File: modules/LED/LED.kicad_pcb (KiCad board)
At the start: 2 copper layers, 40.6 x 40.6 mm, 54 parts, among them J1 2, J10 11, J11 12, J12 13, J13 A0, J14 A1, J15 A2, J16 A3, J17 A4, J18 A5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

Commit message: Fix 74LS139 pins
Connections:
- U2 pad 13: /A0 -> /A1
- U2 pad 14: /A1 -> /A0
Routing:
- net /A1: track 17.6 -> 12.7 mm, vias 2 -> 0
- net /A0: track 11.5 -> 10.2 mm
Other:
- board text added: "07.11.2020"
- board text added: "v2.1"
- board text removed: "08.04.2020"
- board text removed: "v2"

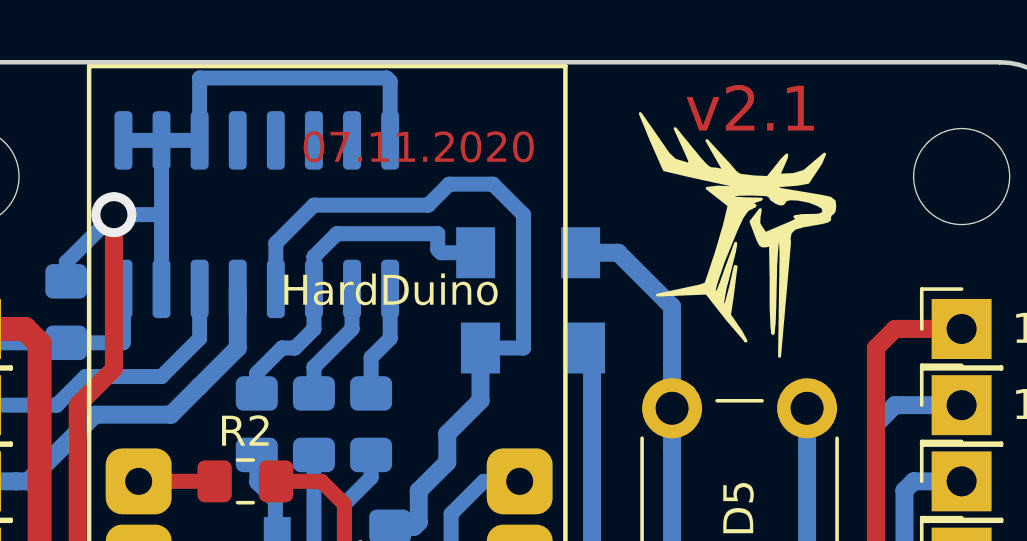
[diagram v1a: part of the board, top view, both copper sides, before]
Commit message: Add hash, fix labels
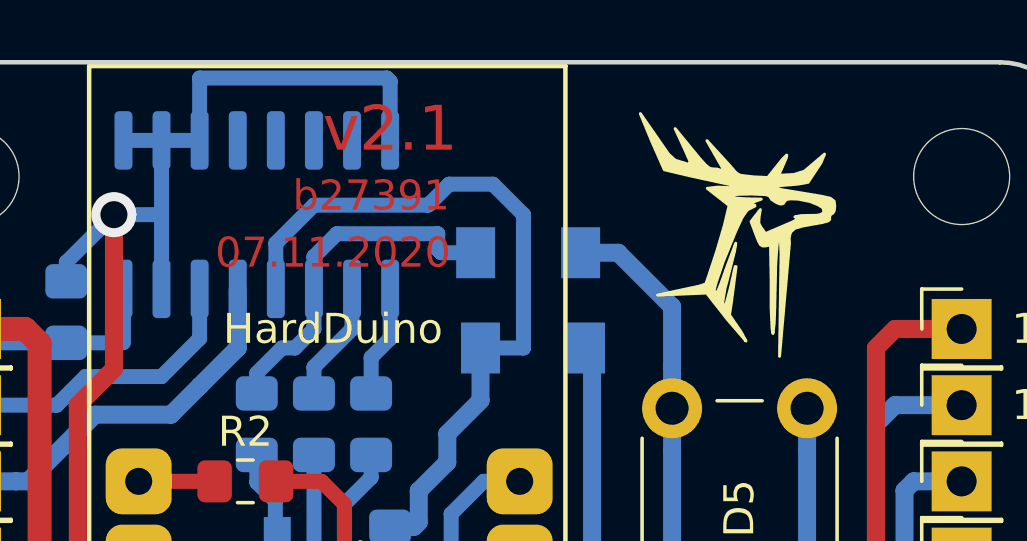
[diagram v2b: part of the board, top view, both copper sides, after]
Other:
- board text added: "b27391"

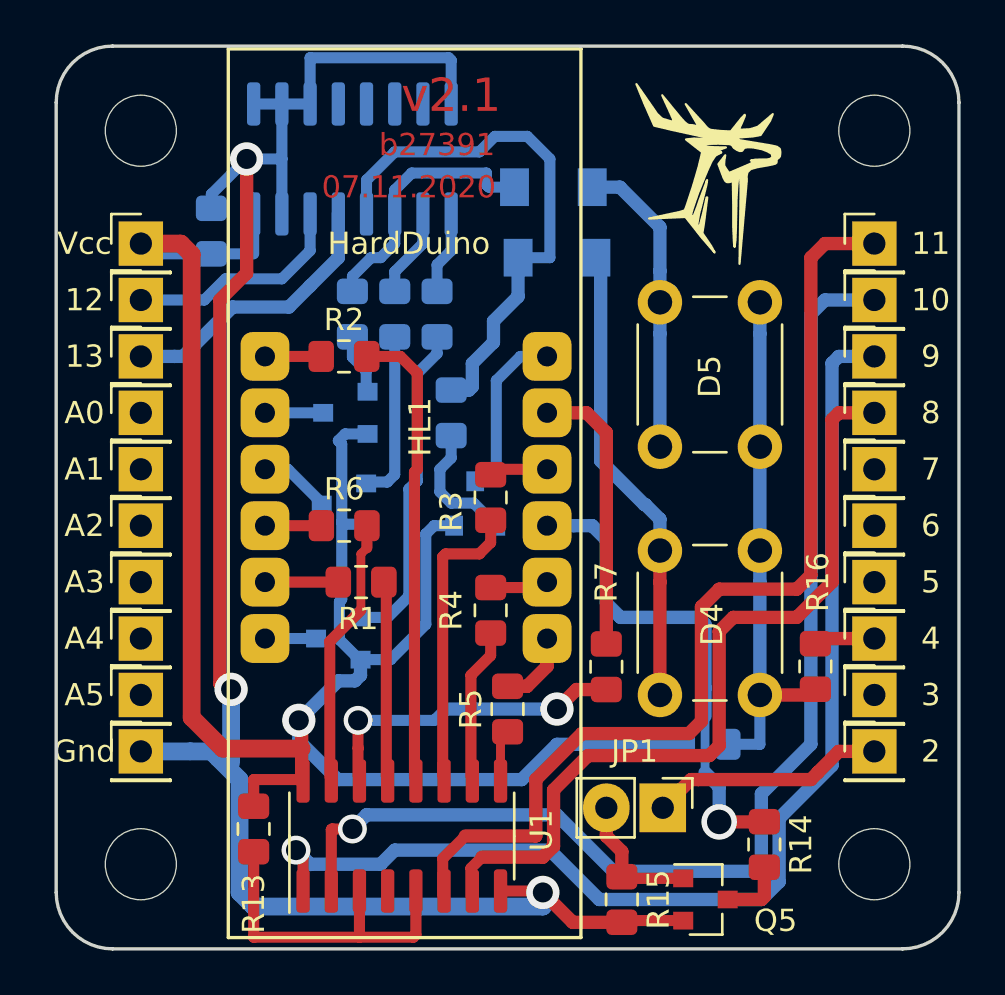
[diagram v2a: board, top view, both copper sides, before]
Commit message: Add legend to LED
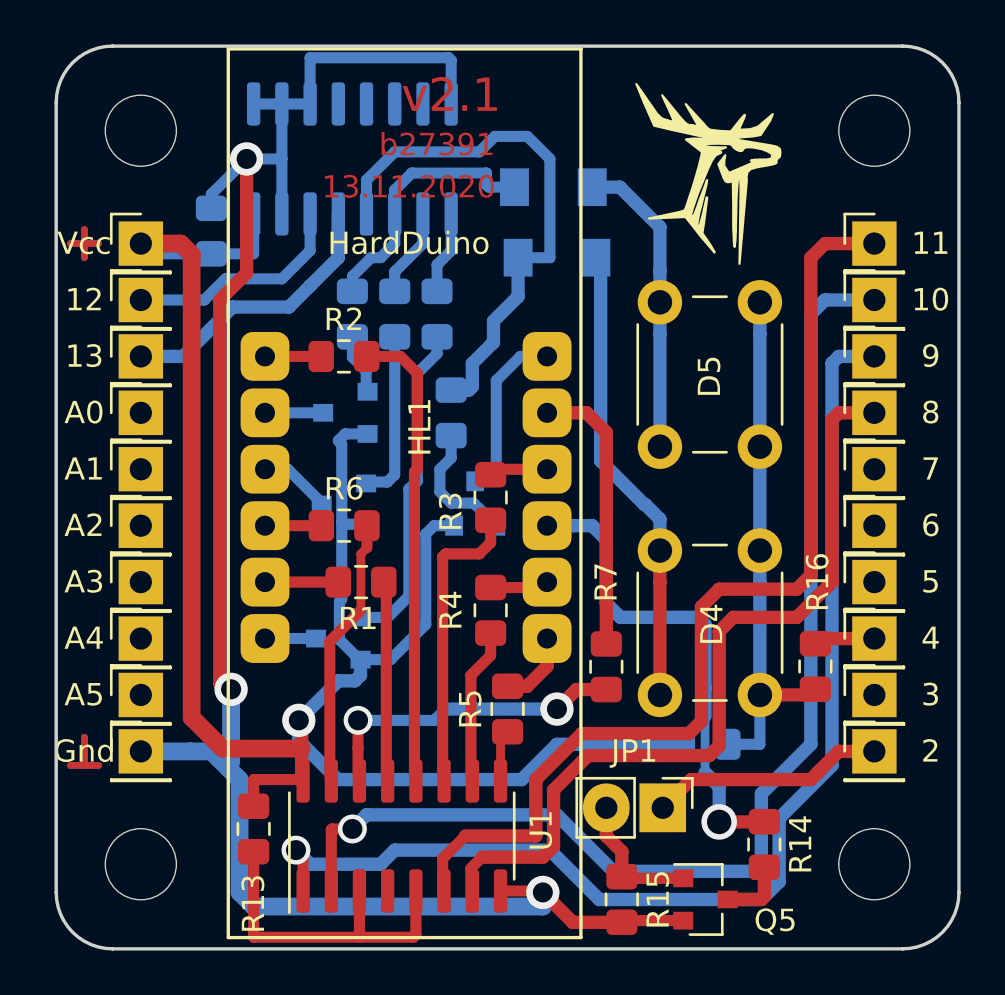
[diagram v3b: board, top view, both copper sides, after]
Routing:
- net (no net): track 0.00 -> 10.2 mm
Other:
- rule solder_mask_min_width: 0.25 -> 0.1
- board text added: "13.11.2020"
- board text added: "D0"
- board text added: "D1"
- board text added: "D2"
- board text added: "D3"
- board text added: "DP"
- board text added: "L0"
- board text removed: "07.11.2020"
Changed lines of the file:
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@@
   (general
     (thickness 1.6)
-    (drawings 33)
-    (tracks 319)
+    (drawings 41)
+    (tracks 327)
     (zones 0)
     (modules 54)
@@
     (pad_drill 1)
     (pad_to_mask_clearance 0.051)
-    (solder_mask_min_width 0.25)
+    (solder_mask_min_width 0.1)
     (aux_axis_origin 0 0)
     (visible_elements 7FFFFFFF)
@@
     )
   )
+  (gr_text A1 (at 90.17 64.77) (layer B.SilkS)
+    (effects (font (size 1 1) (thickness 0.15)) (justify mirror))
+  )
+  (gr_text A0 (at 90.17 62.23) (layer B.SilkS)
+    (effects (font (size 1 1) (thickness 0.15)) (justify mirror))
+  )
+  (gr_text D3 (at 127.9525 59.69) (layer B.SilkS)
+    (effects (font (size 1 1) (thickness 0.15)) (justify mirror))
+  )
+  (gr_text D2 (at 127.9525 62.23) (layer B.SilkS)
+    (effects (font (size 1 1) (thickness 0.15)) (justify mirror))
+  )
+  (gr_text D1 (at 127.9525 64.77) (layer B.SilkS)
+    (effects (font (size 1 1) (thickness 0.15)) (justify mirror))
+  )
+  (gr_text D0 (at 127.9525 67.31) (layer B.SilkS)
+    (effects (font (size 1 1) (thickness 0.15)) (justify mirror))
+  )
+  (gr_text L0 (at 128.27 77.47) (layer B.SilkS)
+    (effects (font (size 1 1) (thickness 0.15)) (justify mirror))
+  )
+  (gr_text DP (at 128.27 82.55) (layer B.SilkS)
+    (effects (font (size 1 1) (thickness 0.15)) (justify mirror))
+  )
   (gr_text b27391 (at 106.045 55.245) (layer F.Cu)
     (effects (font (size 1 1) (thickness 0.2)))
   )
-  (gr_text 07.11.2020 (at 104.775 57.15) (layer F.Cu)
+  (gr_text 13.11.2020 (at 104.775 57.15) (layer F.Cu)
     (effects (font (size 1 1) (thickness 0.2)))
   )
@@
   (gr_line (start 129.54 53.34) (end 129.54 88.9) (layer Edge.Cuts) (width 0.15))
   (gr_line (start 91.44 50.8) (end 127 50.8) (layer Edge.Cuts) (width 0.15))
+  (segment (start 90.17 81.915) (end 90.17 83.185) (width 0.3) (layer B.Cu) (net 0))
+  (segment (start 89.535 83.185) (end 90.805 83.185) (width 0.3) (layer B.Cu) (net 0))
+  (segment (start 90.17 81.915) (end 90.17 83.185) (width 0.3) (layer F.Cu) (net 0))
+  (segment (start 89.535 83.185) (end 90.805 83.185) (width 0.3) (layer F.Cu) (net 0))
+  (segment (start 90.17 59.055) (end 90.17 60.325) (width 0.3) (layer F.Cu) (net 0))
+  (segment (start 89.535 59.69) (end 90.805 59.69) (width 0.3) (layer F.Cu) (net 0))
+  (segment (start 89.535 59.69) (end 90.805 59.69) (width 0.3) (layer B.Cu) (net 0))
+  (segment (start 90.17 59.055) (end 90.17 60.325) (width 0.3) (layer B.Cu) (net 0))
   (segment (start 111.125 60.325) (end 109.6925 60.325) (width 0.5) (layer B.Cu) (net 8))
   (segment (start 111.125 55.88) (end 111.125 60.325) (width 0.5) (layer B.Cu) (net 8))

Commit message: Fix hash, add gerber
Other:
- board text added: "77012c"
- board text removed: "b27391"

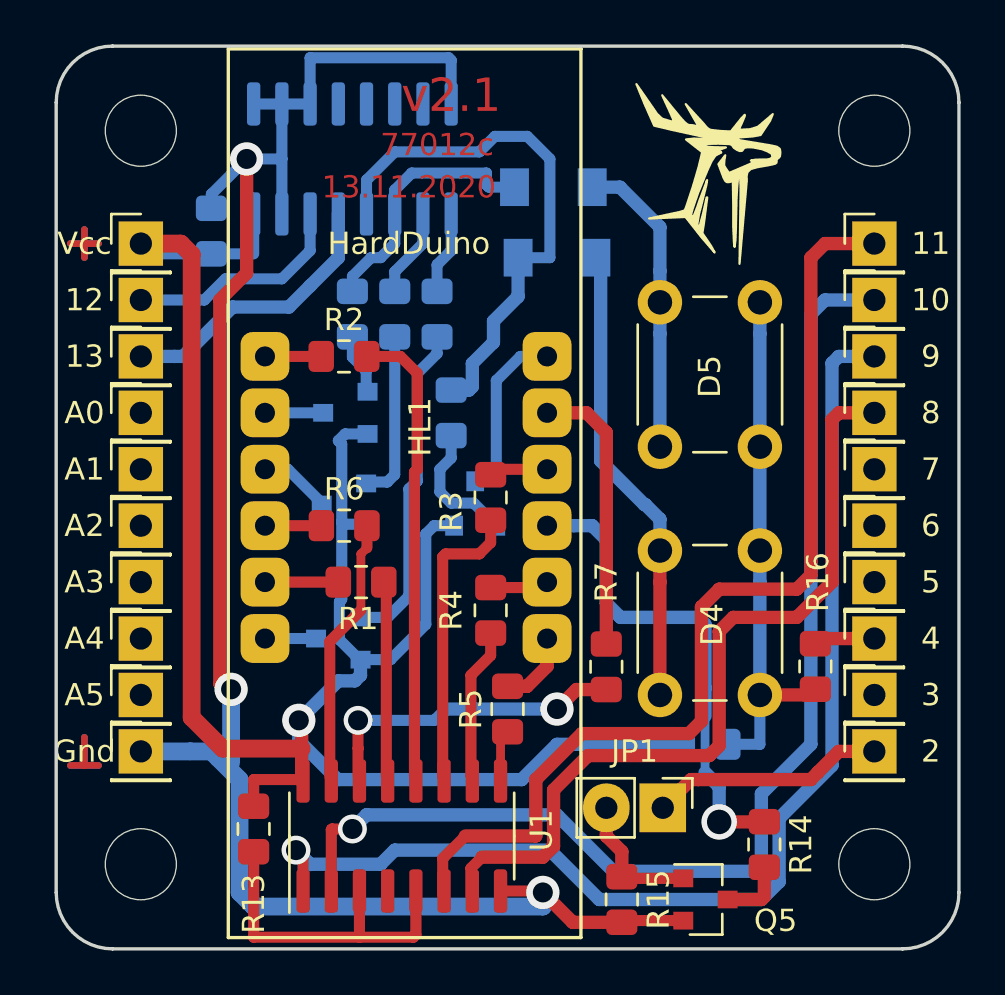
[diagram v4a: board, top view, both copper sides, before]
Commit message: LED. IC names is added.
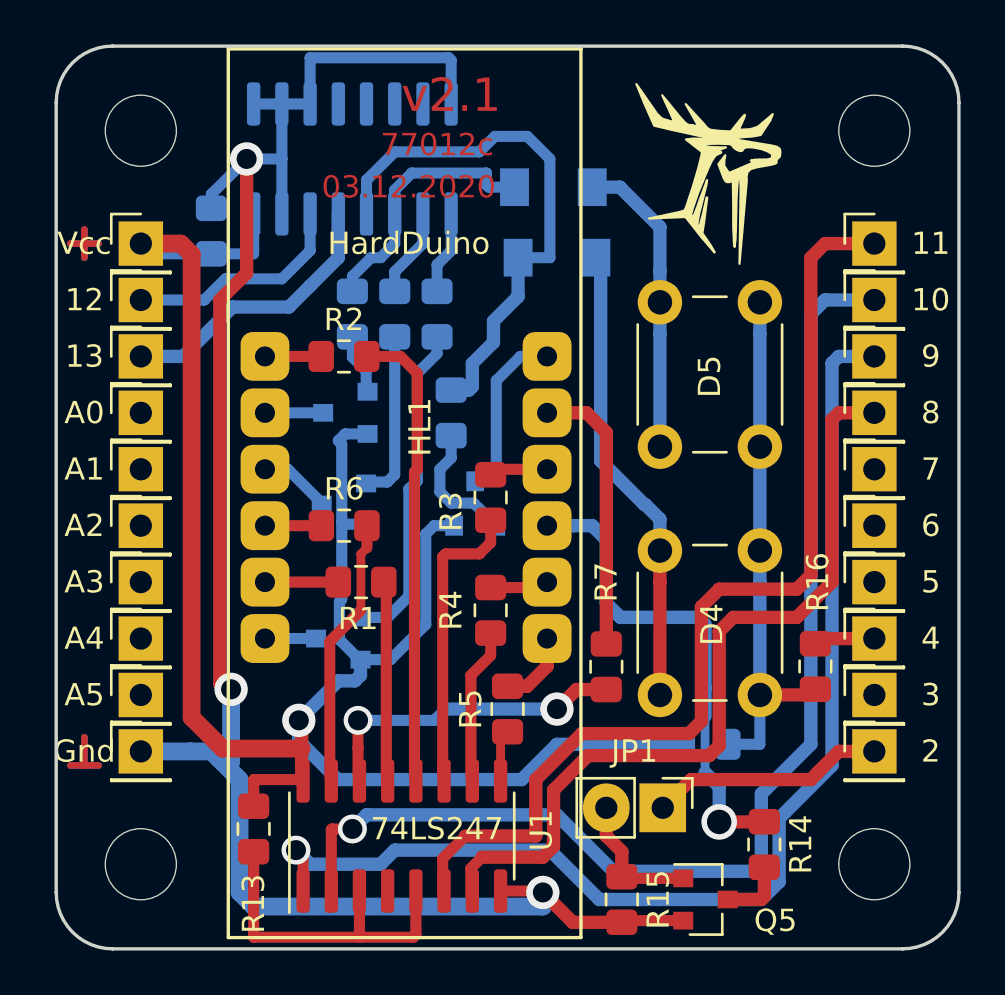
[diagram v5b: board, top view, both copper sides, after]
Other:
- board text added: "03.12.2020"
- board text added: "74HC139"
- board text added: "74LS247"
- board text removed: "13.11.2020"

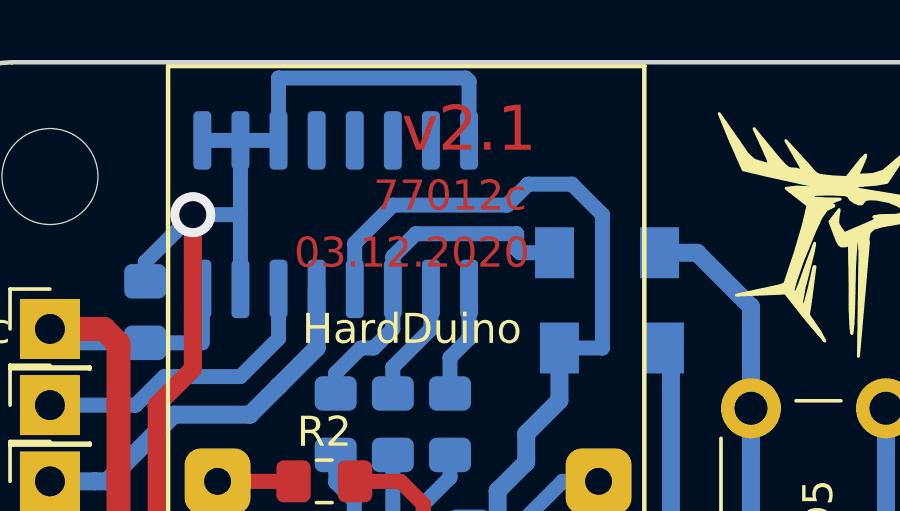
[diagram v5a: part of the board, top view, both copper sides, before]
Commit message: LED. Fix hash, add gerber.
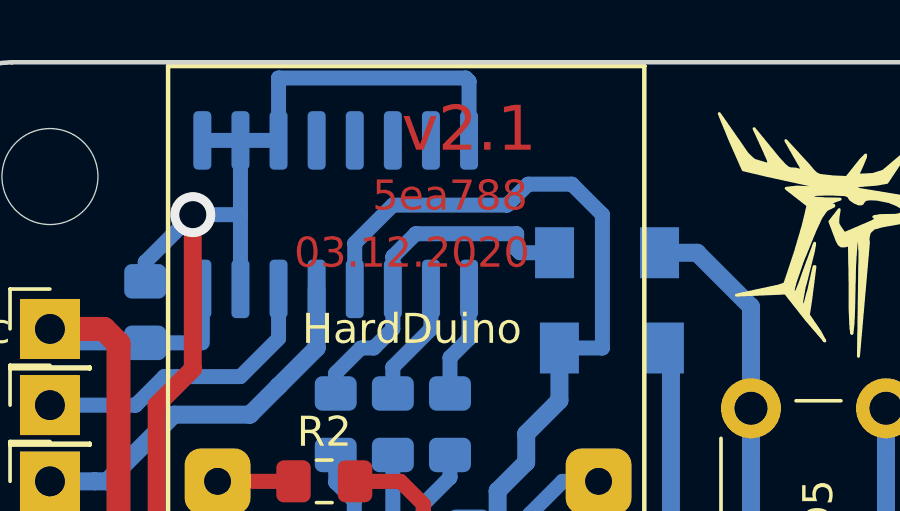
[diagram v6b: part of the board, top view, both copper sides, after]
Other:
- board text added: "5ea788"
- board text removed: "77012c"

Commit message: Fix hash, add gerber
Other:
- board text added: "6c673c"
- board text removed: "5ea788"

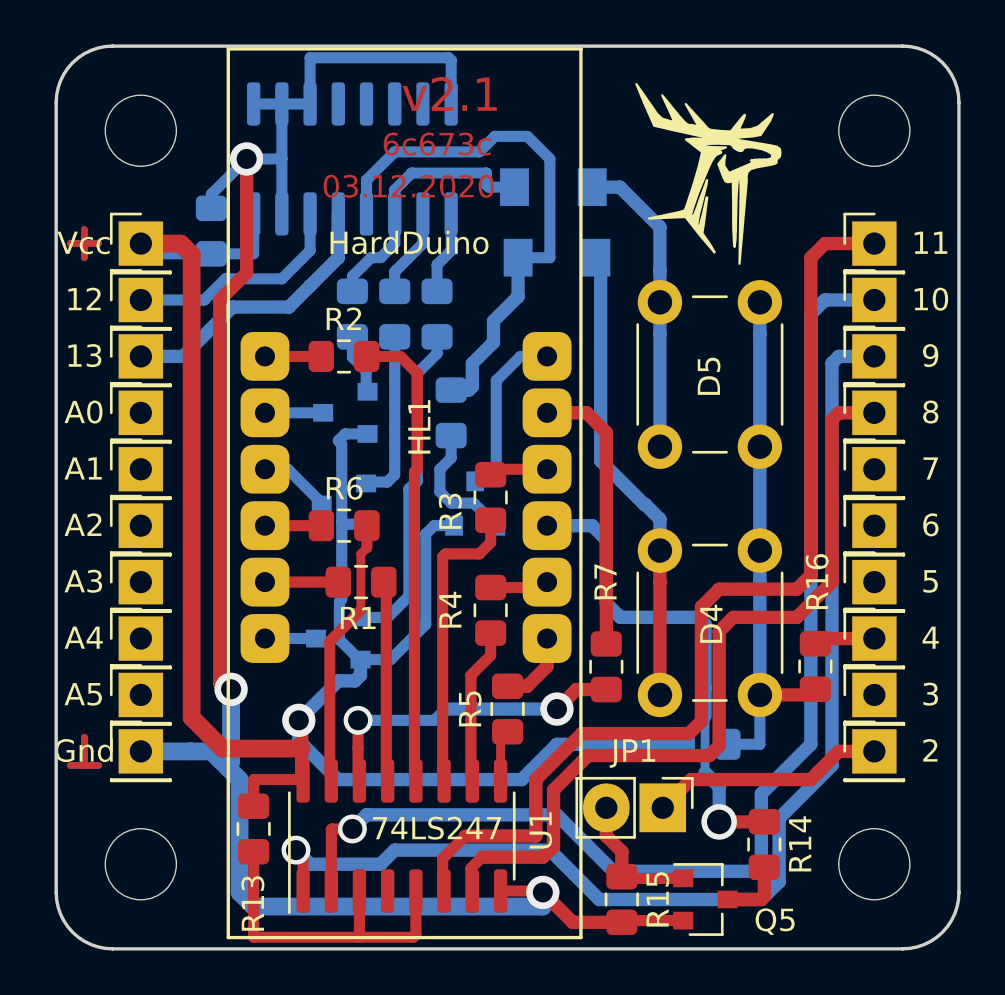
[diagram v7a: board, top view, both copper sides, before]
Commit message: 1x PCBs. Move holes to edges. Caution! This changes is uncompatible with previous versions...
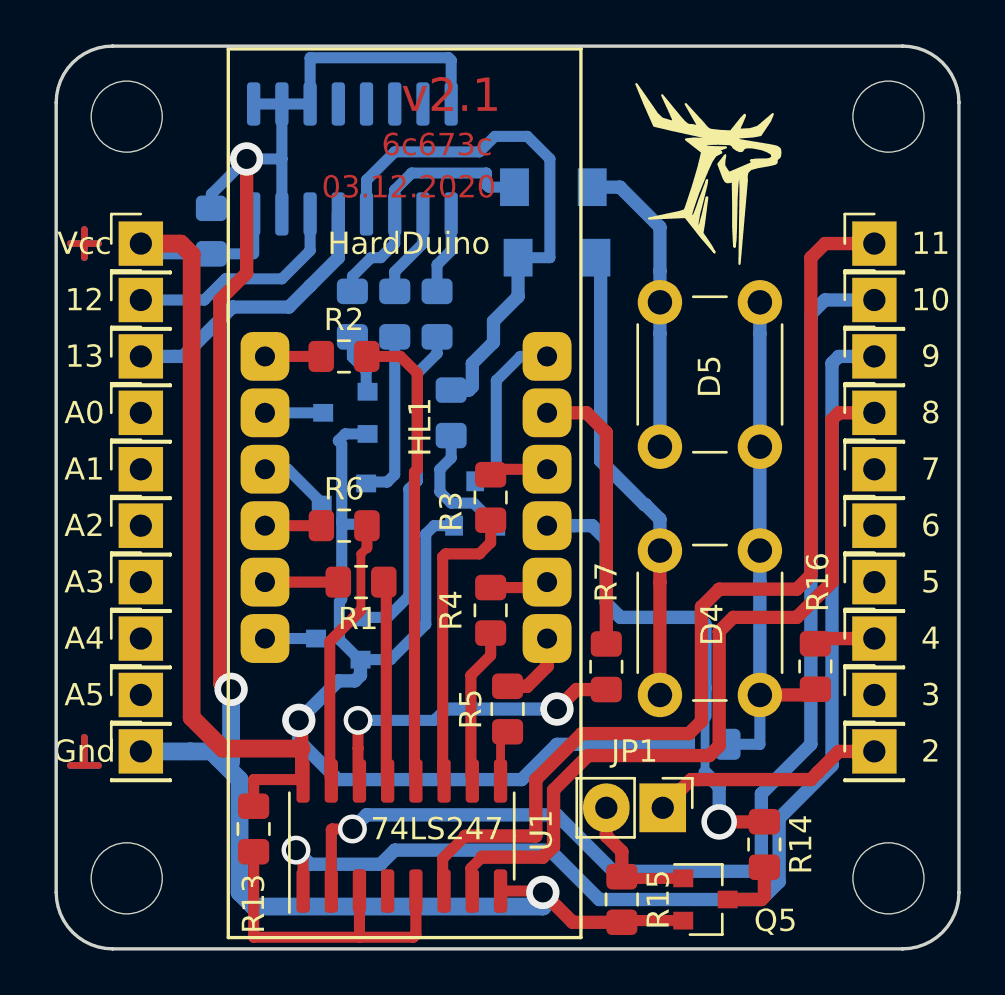
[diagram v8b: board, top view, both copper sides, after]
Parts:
- moved H2 0.90 mm to (92.1, 88.3)
- moved H4 0.90 mm to (126.4, 88.3)
- moved H1 0.90 mm to (92.1, 54.0)
- moved H3 0.90 mm to (126.4, 54.0)
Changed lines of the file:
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@@
   )
   (module MountingHole:MountingHole_3.2mm_M3 (layer F.Cu)
-    (at 92.71 54.61)
+    (at 92.0750 53.9750)
     (descr "Mounting Hole 3.2mm, no annular, M3")
     (tags "mounting hole 3.2mm no annular m3")
@@
   )
   (module MountingHole:MountingHole_3.2mm_M3 (layer F.Cu)
-    (at 92.71 87.63)
+    (at 92.0750 88.2650)
     (descr "Mounting Hole 3.2mm, no annular, M3")
     (tags "mounting hole 3.2mm no annular m3")
@@
   )
   (module MountingHole:MountingHole_3.2mm_M3 (layer F.Cu)
-    (at 125.73 54.61)
+    (at 126.3650 53.9750)
     (descr "Mounting Hole 3.2mm, no annular, M3")
     (tags "mounting hole 3.2mm no annular m3")
@@
   )
   (module MountingHole:MountingHole_3.2mm_M3 (layer F.Cu)
-    (at 125.73 87.63)
+    (at 126.3650 88.2650)
     (descr "Mounting Hole 3.2mm, no annular, M3")
     (tags "mounting hole 3.2mm no annular m3")
